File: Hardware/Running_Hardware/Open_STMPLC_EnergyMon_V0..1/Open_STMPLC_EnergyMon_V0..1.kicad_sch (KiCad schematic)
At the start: 122 parts, among them J1 Conn_02x08_Odd_Even, J2 Screw_Terminal_01x08, U1 ATM90E36A, U2 ISO7762FDBQ, U5 AMS1117-3.3, Y1 16.384MHz

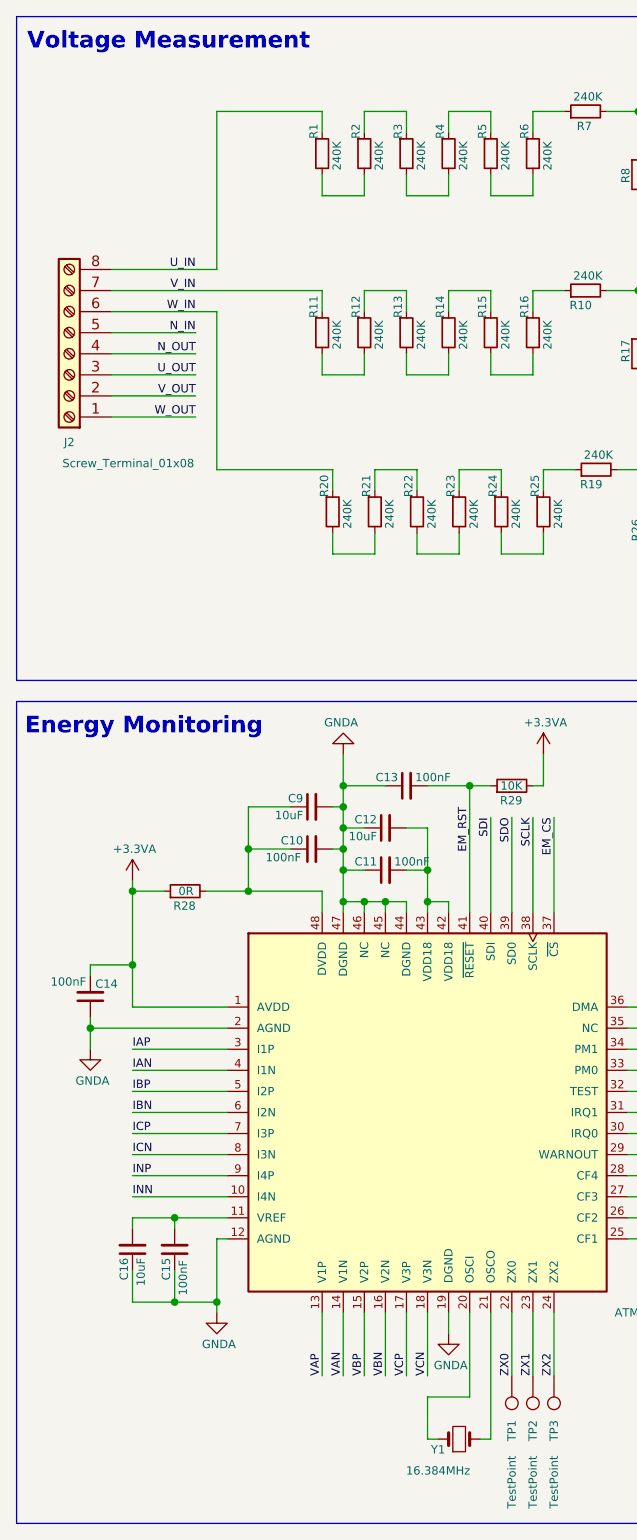
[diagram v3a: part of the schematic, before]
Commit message: Energy monitoring component grouping
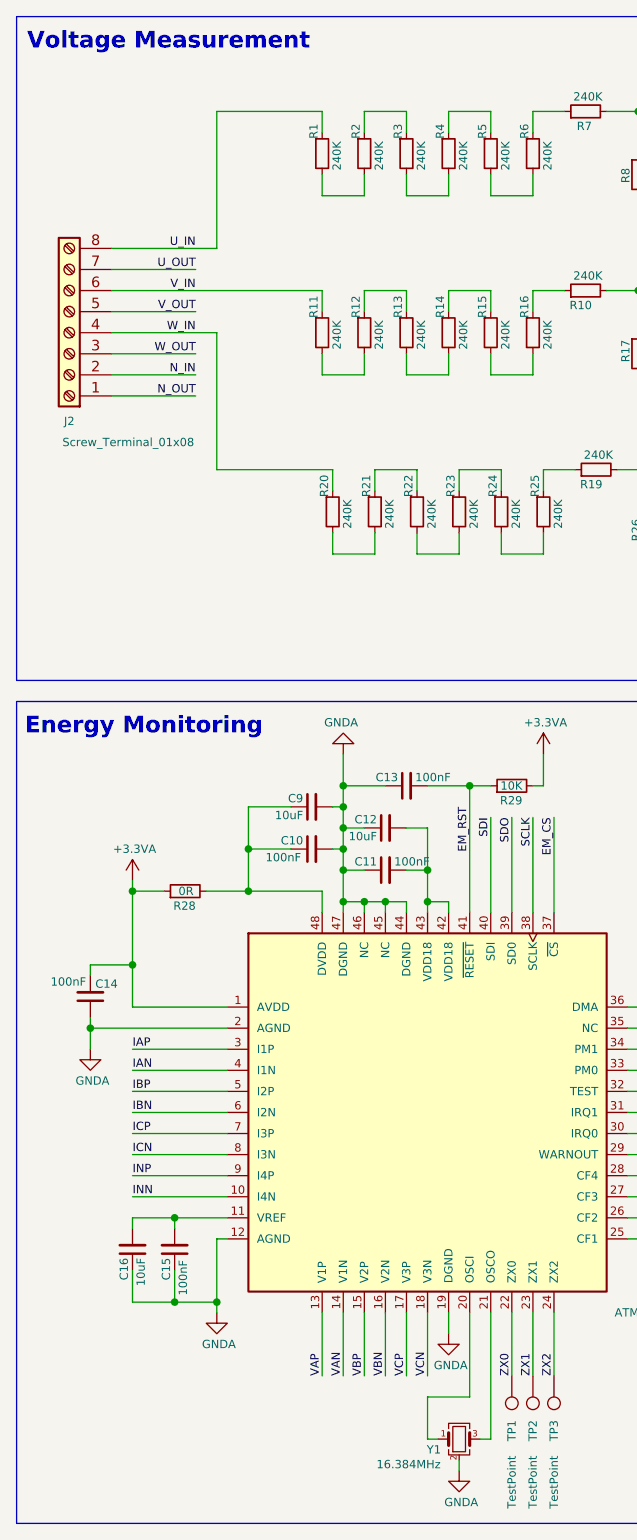
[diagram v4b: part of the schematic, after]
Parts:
- C10, C11, C13, C14, C15: footprint Capacitor_SMD:C_0805_2012Metric_Pad1.18x1.45mm_HandSolder -> Capacitor_SMD:C_0603_1608Metric_Pad1.08x0.95mm_HandSolder
- J2: footprint TerminalBlock_Phoenix:TerminalBlock_Phoenix_MKDS-1,5-8-5.08_1x08_P5.08mm_Horizontal -> TerminalBlock_Phoenix:TerminalBlock_Phoenix_MKDS-1-8-3.81_1x08_P3.81mm_Horizontal
- Y1: symbol Device:Crystal_Small -> Device:Crystal_GND24_Small
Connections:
- net GNDA: now also Y1.2 (G), Y1.4 (G)
- net N_IN: now also J2.2 (Pin_2); no longer J2.5 (Pin_5)
- net N_OUT: now also J2.1 (Pin_1); no longer J2.4 (Pin_4)
- net U_OUT: now also J2.7 (Pin_7); no longer J2.3 (Pin_3)
- net V_IN: now also J2.6 (Pin_6); no longer J2.7 (Pin_7)
- net V_OUT: now also J2.5 (Pin_5); no longer J2.2 (Pin_2)
- net W_IN: now also J2.4 (Pin_4); no longer J2.6 (Pin_6)
- net W_OUT: now also J2.3 (Pin_3); no longer J2.1 (Pin_1)
- net at U1.21 (OSCO): now also Y1.3; no longer Y1.2
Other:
- moved on the sheet: J2
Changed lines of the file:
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@@
 	(wire
 		(pts
-			(xy 38.1 49.53) (xy 38.1 68.58)
-		)
-		(stroke
-			(width 0)
-			(type default)
-		)
-	)
-	(wire
-		(pts
 			(xy 33.02 158.75) (xy 39.37 158.75)
 		)
@@
 	(wire
 		(pts
-			(xy 25.4 44.45) (xy 38.1 44.45)
+			(xy 25.4 41.91) (xy 38.1 41.91)
 		)
 		(stroke
@@
 	(wire
 		(pts
-			(xy 25.4 57.15) (xy 35.56 57.15)
+			(xy 25.4 44.45) (xy 35.56 44.45)
 		)
 		(stroke
@@
 	(wire
 		(pts
+			(xy 25.4 57.15) (xy 35.56 57.15)
+		)
+		(stroke
+			(width 0)
+			(type default)
+		)
+	)
+	(wire
+		(pts
 			(xy 96.52 80.01) (xy 104.14 80.01)
 		)
@@
 	(wire
 		(pts
+			(xy 25.4 46.99) (xy 50.8 46.99)
+		)
+		(stroke
+			(width 0)
+			(type default)
+		)
+	)
+	(wire
+		(pts
 			(xy 38.1 68.58) (xy 52.07 68.58)
 		)
@@
 	(wire
 		(pts
-			(xy 25.4 46.99) (xy 50.8 46.99)
-		)
-		(stroke
-			(width 0)
-			(type default)
-		)
-	)
-	(wire
-		(pts
 			(xy 53.34 170.18) (xy 53.34 177.8)
 		)
@@
 	(wire
 		(pts
+			(xy 25.4 52.07) (xy 38.1 52.07)
+		)
+		(stroke
+			(width 0)
+			(type default)
+		)
+	)
+	(wire
+		(pts
 			(xy 90.17 68.58) (xy 96.52 68.58)
 		)
@@
 	(wire
 		(pts
-			(xy 38.1 44.45) (xy 38.1 25.4)
+			(xy 38.1 41.91) (xy 38.1 25.4)
 		)
 		(stroke
@@
 	(wire
 		(pts
-			(xy 25.4 52.07) (xy 35.56 52.07)
-		)
-		(stroke
-			(width 0)
-			(type default)
-		)
-	)
-	(wire
-		(pts
 			(xy 264.16 153.67) (xy 267.97 153.67)
 		)
@@
 	(wire
 		(pts
-			(xy 25.4 62.23) (xy 35.56 62.23)
+			(xy 25.4 54.61) (xy 35.56 54.61)
 		)
 		(stroke
@@
 	(wire
 		(pts
+			(xy 38.1 68.58) (xy 38.1 52.07)
+		)
+		(stroke
+			(width 0)
+			(type default)
+		)
+	)
+	(wire
+		(pts
 			(xy 68.58 106.68) (xy 63.5 106.68)
 		)
@@
 	(wire
 		(pts
-			(xy 251.46 68.58) (xy 246.38 68.58)
+			(xy 67.31 187.96) (xy 67.31 189.23)
 		)
 		(stroke
@@
 	(wire
 		(pts
-			(xy 85.09 25.4) (xy 88.9 25.4)
+			(xy 251.46 68.58) (xy 246.38 68.58)
 		)
 		(stroke
@@
 	(wire
 		(pts
-			(xy 76.2 54.61) (xy 76.2 57.15)
+			(xy 85.09 25.4) (xy 88.9 25.4)
 		)
 		(stroke
@@
 	(wire
 		(pts
-			(xy 210.82 119.38) (xy 218.44 119.38)
+			(xy 76.2 54.61) (xy 76.2 57.15)
 		)
 		(stroke
@@
 	(wire
 		(pts
-			(xy 208.28 134.62) (xy 224.79 134.62)
+			(xy 210.82 119.38) (xy 218.44 119.38)
 		)
 		(stroke
@@
 	(wire
 		(pts
-			(xy 25.4 49.53) (xy 38.1 49.53)
+			(xy 208.28 134.62) (xy 224.79 134.62)
 		)
 		(stroke
@@
 	(wire
 		(pts
-			(xy 25.4 54.61) (xy 35.56 54.61)
+			(xy 25.4 59.69) (xy 35.56 59.69)
 		)
 		(stroke
@@
 	(wire
 		(pts
-			(xy 25.4 59.69) (xy 35.56 59.69)
+			(xy 25.4 49.53) (xy 35.56 49.53)
 		)
 		(stroke
@@
 	)
 	(label "W_IN"
-		(at 35.56 49.53 180)
+		(at 35.56 52.07 180)
 		(effects
 			(font
@@
 	)
 	(label "U_IN"
-		(at 35.56 44.45 180)
+		(at 35.56 41.91 180)
 		(effects
 			(font
@@
 	)
 	(label "U_OUT"
-		(at 35.56 57.15 180)
+		(at 35.56 44.45 180)
 		(effects
 			(font
@@
 	)
 	(label "V_OUT"
-		(at 35.56 59.69 180)
+		(at 35.56 49.53 180)
 		(effects
 			(font
@@
 	)
 	(label "N_IN"
-		(at 35.56 52.07 180)
+		(at 35.56 57.15 180)
 		(effects
 			(font
@@
 	)
 	(label "N_OUT"
-		(at 35.56 54.61 180)
+		(at 35.56 59.69 180)
 		(effects
 			(font
@@
 	)
 	(label "W_OUT"
-		(at 35.56 62.23 180)
+		(at 35.56 54.61 180)
 		(effects
 			(font
@@
 			)
 		)
-		(property "Footprint" "Capacitor_SMD:C_0805_2012Metric_Pad1.18x1.45mm_HandSolder"
+		(property "Footprint" "Capacitor_SMD:C_0603_1608Metric_Pad1.08x0.95mm_HandSolder"
 			(at 60.96 106.68 0)
 			(effects
@@
 			)
 		)
-		(property "Footprint" "Capacitor_SMD:C_0805_2012Metric_Pad1.18x1.45mm_HandSolder"
+		(property "Footprint" "Capacitor_SMD:C_0603_1608Metric_Pad1.08x0.95mm_HandSolder"
 			(at 49.53 114.3 0)
 			(effects
@@
 			)
 		)
-		(property "Footprint" "Capacitor_SMD:C_0805_2012Metric_Pad1.18x1.45mm_HandSolder"
+		(property "Footprint" "Capacitor_SMD:C_0603_1608Metric_Pad1.08x0.95mm_HandSolder"
 			(at 58.42 116.84 0)
 			(effects
@@
 			)
 		)
-		(property "Footprint" "Capacitor_SMD:C_0805_2012Metric_Pad1.18x1.45mm_HandSolder"
+		(property "Footprint" "Capacitor_SMD:C_0603_1608Metric_Pad1.08x0.95mm_HandSolder"
 			(at 33.02 162.56 0)
 			(effects
@@
 	)
 	(symbol
-		(lib_id "Device:Crystal_Small")
+		(lib_id "Device:Crystal_GND24_Small")
 		(at 67.31 185.42 0)
 		(unit 1)
@@
 		(dnp no)
 		(property "Reference" "Y1"
-			(at 64.77 186.69 0)
+			(at 64.262 186.69 0)
 			(effects
 				(font
@@
 		)
 		(property "Value" "16.384MHz"
-			(at 64.77 189.23 0)
+			(at 61.214 188.468 0)
 			(effects
 				(font
@@
 			)
 		)
-		(property "Description" "Two pin crystal, small symbol"
+		(property "Description" "Four pin crystal, GND on pins 2 and 4, small symbol"
 			(at 67.31 185.42 0)
 			(effects
@@
 		(pin "1"
 		)
+		(pin "3"
+		)
+		(pin "4"
+		)
 		(instances
 			(project "Open_STMPLC_EnergyMon_V0..1"
@@
 			)
 		)
-		(property "Footprint" "Capacitor_SMD:C_0805_2012Metric_Pad1.18x1.45mm_HandSolder"
+		(property "Footprint" "Capacitor_SMD:C_0603_1608Metric_Pad1.08x0.95mm_HandSolder"
 			(at 22.86 132.08 0)
 			(effects
@@
 	)
 	(symbol
+		(lib_id "power:GNDA")
+		(at 67.31 189.23 0)
+		(unit 1)
+		(exclude_from_sim no)
+		(in_bom yes)
+		(on_board yes)
+		(dnp no)
+		(property "Reference" "#PWR036"
+			(at 67.31 195.58 0)
+			(effects
+				(font
+					(size 1 1)
+				)
+				(hide yes)
+			)
+		)
+		(property "Value" "GNDA"
+			(at 67.564 193.04 0)
+			(effects
+				(font
+					(size 1 1)
+				)
+			)
+		)
+		(property "Footprint" ""
+			(at 67.31 189.23 0)
+			(effects
+				(font
+					(size 1.27 1.27)
+				)
+				(hide yes)
+			)
+		)
+		(property "Datasheet" ""
+			(at 67.31 189.23 0)
+			(effects
+				(font
+					(size 1.27 1.27)
+				)
+				(hide yes)
+			)
+		)
+		(property "Description" "Power symbol creates a global label with name \"GNDA\" , analog ground"
+			(at 67.31 189.23 0)
+			(effects
+				(font
+					(size 1.27 1.27)
+				)
+				(hide yes)
+			)
+		)
+		(pin "1"
+		)
+		(instances
+			(project "Open_STMPLC_EnergyMon_V0..1"
+				(path "/fbd19ffd-5bb3-40ce-9c19-bcf6847c5c31"
+					(reference "#PWR036")
+					(unit 1)
+				)
+			)
+		)
+	)
+	(symbol
 		(lib_id "Device:C_Small")
 		(at 109.22 54.61 0)
@@
 	(symbol
 		(lib_id "Connector:Screw_Terminal_01x08")
-		(at 20.32 54.61 180)
+		(at 20.32 52.07 180)
 		(unit 1)
 		(exclude_from_sim no)
@@
 		(dnp no)
 		(property "Reference" "J2"
-			(at 20.32 65.278 0)
+			(at 20.32 62.738 0)
 			(effects
 				(font
@@
 		)
 		(property "Value" "Screw_Terminal_01x08"
-			(at 27.432 67.818 0)
+			(at 27.432 65.278 0)
 			(effects
 				(font
@@
 			)
 		)
-		(property "Footprint" "TerminalBlock_Phoenix:TerminalBlock_Phoenix_MKDS-1,5-8-5.08_1x08_P5.08mm_Horizontal"
-			(at 20.32 54.61 0)
+		(property "Footprint" "TerminalBlock_Phoenix:TerminalBlock_Phoenix_MKDS-1-8-3.81_1x08_P3.81mm_Horizontal"
+			(at 20.32 52.07 0)
 			(effects
 				(font
@@
 		)
 		(property "Datasheet" "~"
-			(at 20.32 54.61 0)
+			(at 20.32 52.07 0)
 			(effects
 				(font
@@
 		)
 		(property "Description" "Generic screw terminal, single row, 01x08, script generated (kicad-library-utils/schlib/autogen/connector/)"
-			(at 20.32 54.61 0)
+			(at 20.32 52.07 0)
 			(effects
 				(font

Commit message: Energy monitoring layout
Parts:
- added H1, H2, H3, H4: MountingHole, MountingHole:MountingHole_3.2mm_M3, symbol Mechanical:MountingHole
- J1: footprint Connector_PinSocket_2.54mm:PinSocket_2x08_P2.54mm_Horizontal -> Connector_PinHeader_2.54mm:PinHeader_2x08_P2.54mm_Horizontal
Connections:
- net EX_GPIO1: now also U2.4 (INC); no longer U2.2 (INA)
- net EX_GPIO3: now also U2.2 (INA); no longer U2.7 (OUTF)
- net EX_SPI_CLK: now also U2.6 (OUTE); no longer U2.5 (IND)
- net EX_SPI_MISO: now also U2.7 (OUTF); no longer U2.6 (OUTE)
- net EX_SPI_MOSI: now also U2.5 (IND); no longer U2.4 (INC)
- net GND: no longer C26.2
- net GNDA: now also C26.2
- net IRQ0: now also U2.13 (OUTC); no longer U2.10 (INF)
- net N_IN: now also J2.8 (Pin_8); no longer J2.2 (Pin_2)
- net N_OUT: now also J2.7 (Pin_7); no longer J2.1 (Pin_1)
- net SCLK: now also U2.11 (INE); no longer U2.12 (OUTD)
- net SDI: now also U2.12 (OUTD); no longer U2.13 (OUTC)
- net SDO: now also U2.10 (INF); no longer U2.11 (INE)
- net U_IN: now also J2.1 (Pin_1); no longer J2.8 (Pin_8)
- net U_OUT: now also J2.2 (Pin_2); no longer J2.7 (Pin_7)
- net V_IN: now also J2.3 (Pin_3); no longer J2.6 (Pin_6)
- net V_OUT: now also J2.4 (Pin_4); no longer J2.5 (Pin_5)
- net W_IN: now also J2.6 (Pin_6); no longer J2.4 (Pin_4)
- net W_OUT: now also J2.5 (Pin_5); no longer J2.3 (Pin_3)
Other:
- moved on the sheet: J2

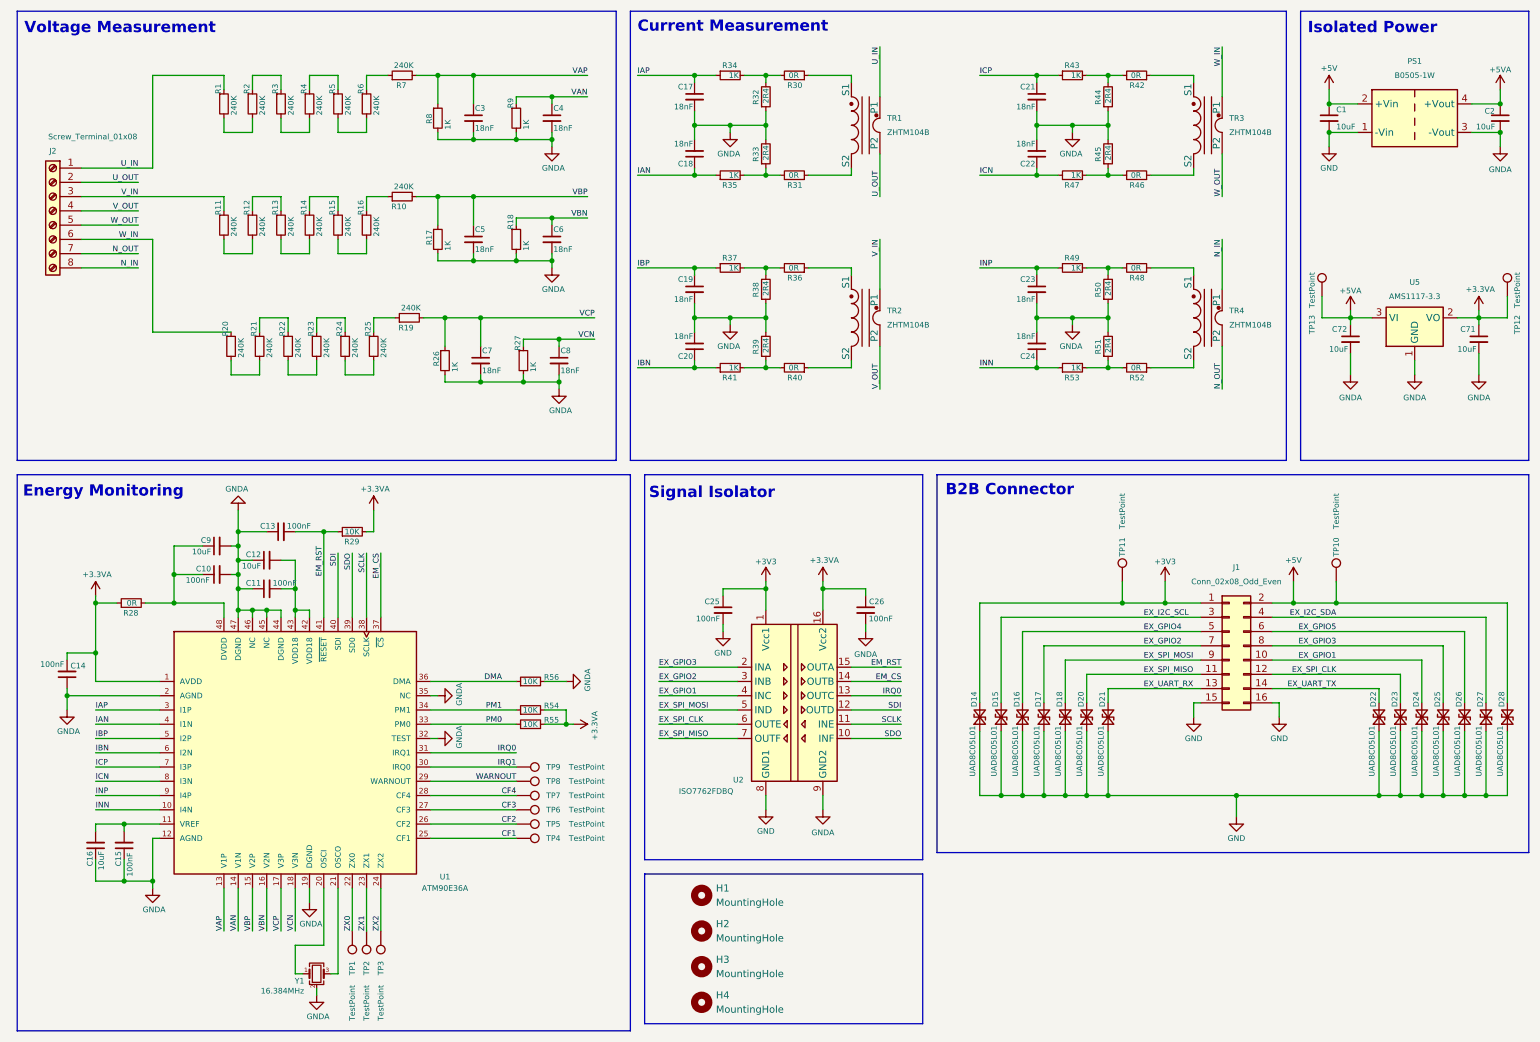
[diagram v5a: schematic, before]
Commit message: Energy monitoring gerber generated
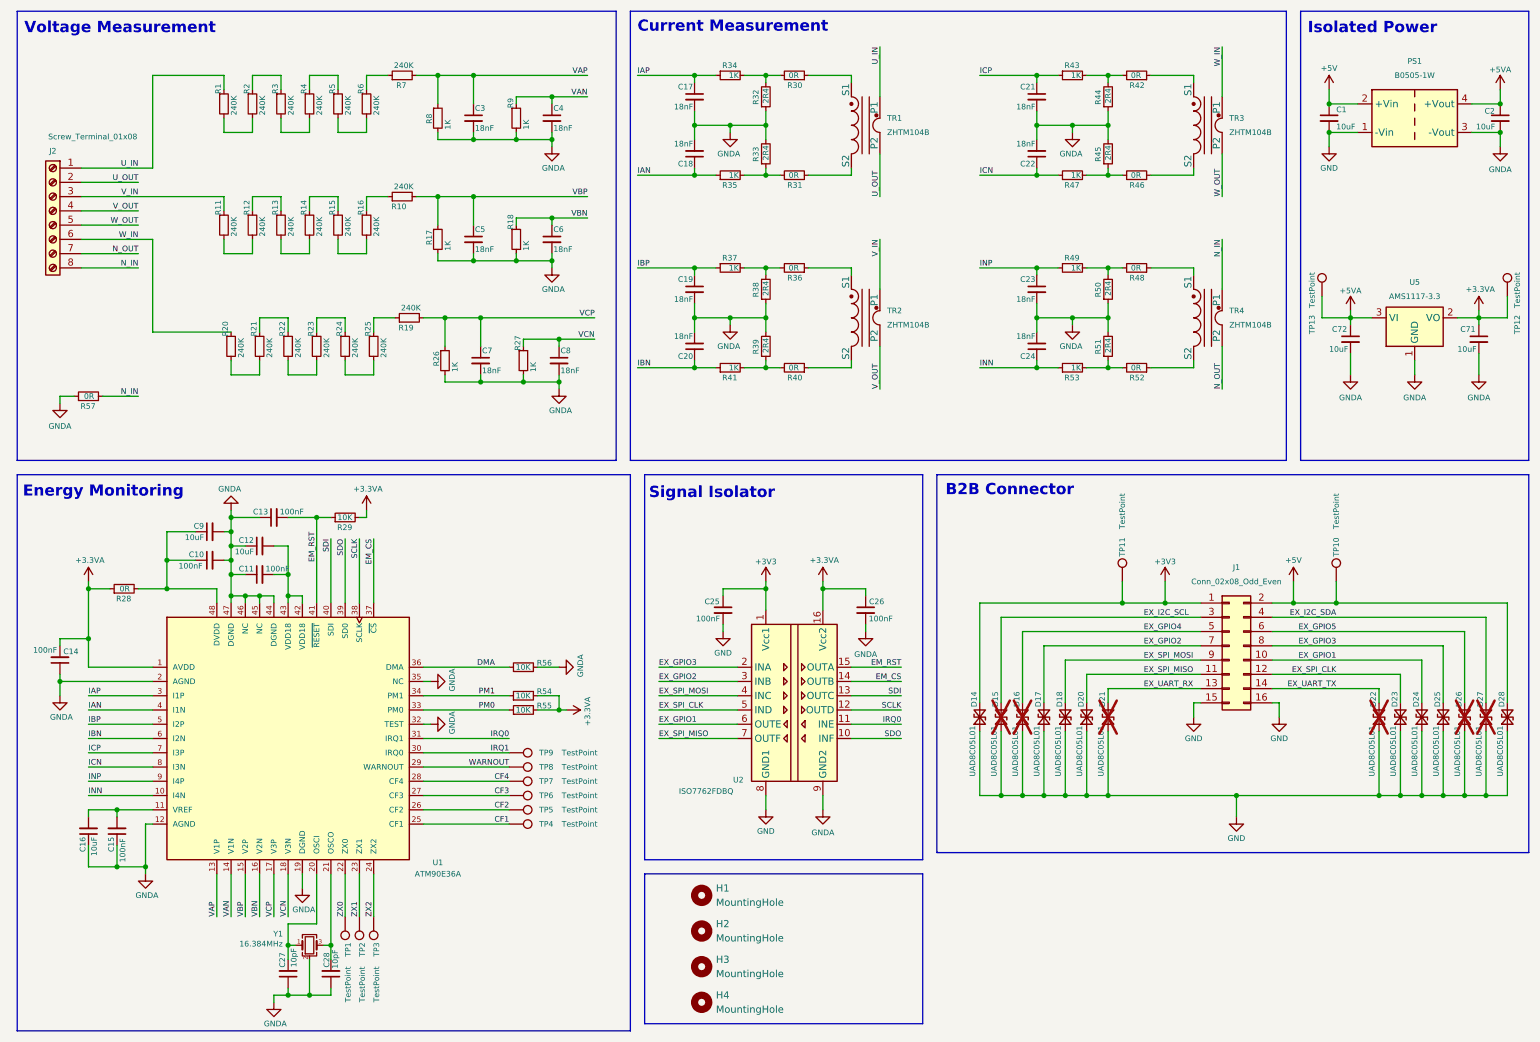
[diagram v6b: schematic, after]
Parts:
- added C27, C28: 10pF, Capacitor_SMD:C_0603_1608Metric_Pad1.08x0.95mm_HandSolder, symbol Device:C_Small
- added R57: 0R, Resistor_SMD:R_0603_1608Metric_Pad0.98x0.95mm_HandSolder, symbol Device:R_Small
- D15, D16, D21, D22, D26, D27: now not fitted
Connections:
- net EX_GPIO1: now also U2.6 (OUTE); no longer U2.4 (INC)
- net EX_SPI_CLK: now also U2.5 (IND); no longer U2.6 (OUTE)
- net EX_SPI_MOSI: now also U2.4 (INC); no longer U2.5 (IND)
- net GNDA: now also C27.1, C28.1, R57.1
- net IRQ0: now also U2.11 (INE); no longer U2.13 (OUTC)
- net N_IN: now also R57.2
- net SCLK: now also U2.12 (OUTD); no longer U2.11 (INE)
- net SDI: now also U2.13 (OUTC); no longer U2.12 (OUTD)
- net at U1.20 (OSCI), Y1.1: now also C27.2
- net at U1.21 (OSCO), Y1.3: now also C28.2
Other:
- company: (none) -> Thingslista Automation LLP
- moved on the sheet: C10, C11, C12, C13, C14, C15, C16, C9, R28, R29, R54, R55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
